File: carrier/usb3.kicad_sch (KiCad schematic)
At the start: 0 parts

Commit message: Feat[carrier]: v3 schematic draft complete
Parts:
- added C25, C26, C30, C31, C32, C37, C40, C41, C42, C43, C44, C45, C48, C51, C52: 10nF, symbol Device:C_Small
- added C3 (x2): 150uF, symbol Device:C_Polarized_Small
- added C38, C39, C46, C47, C49, C50, C54, C55, C56, C57, C58, C59, C9 (x2): 100nF, symbol Device:C_Small
- added C4 (x2), C53: 10uF, symbol Device:C_Small
- added C60, C61: 22pF, symbol Device:C_Small
- added FB1, FB2, FB3: BLM21PG600SN1, symbol Device:FerriteBead_Small
- added J11, J12: USB3_A, symbol Connector:USB3_A
- added R10: 1.6k, symbol Device:R_Small
- added R39: 680, symbol Device:R_Small
- added R40, R43, R45: 10k, symbol Device:R_Small
- added R44: 47k, symbol Device:R_Small
- added R8 (x2): 1M, symbol Device:R_Small
- added U12: uPD720202, Package_DFN_QFN:QFN-48-1EP_7x7mm_P0.5mm_EP5.45x5.45mm, symbol uPD720202:uPD720202
- added U14: W25X40CLUXIG, symbol Memory_Flash:W25X40CLSV
- added U15, U16: AP2191, Package_TO_SOT_SMD:SOT-23-5, symbol AP2191:AP2191
- added U5 (x3): TPD4EUSB30, Package_SON:USON-10_2.5x1.0mm_P0.5mm, symbol CM4IO:TPD4EUSB30
- added Y2: 24MHz, symbol Device:Crystal_GND24_Small
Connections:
- new net: C60.1, R39.1, Y2.3
- new net: C9.1, J12.4 (GND), R8.1
- new net: FB2.2, J11.1 (VBUS)
- new net: C9.1, J11.4 (GND), R8.1
- new net: C56.2, J11.8 (SSTX-)
- new net: C57.2, J11.9 (SSTX+)
- new net: FB3.2, J12.1 (VBUS)
- new net: C58.2, J12.8 (SSTX-)
- new net: C59.2, J12.9 (SSTX+)
- new net: C54.2, U12.4 (PETXP)
- new net: R39.2, U12.23 (XT2)
- new net: C61.1, U12.24 (XT1), Y2.1
- new net: R10.1, U12.26 (RREF)
- new net: C55.2, U12.5 (PETXN)
- new net: R43.2, U14.3 (~{WP})
- new net +1.05v: C39.1, C40.1, C41.1, C42.1, C43.1, C44.1, C45.1, C46.1, C47.1, C48.1, U12.21 (VDD10), U12.30 (VDD10), U12.33 (VDD10), U12.39 (VDD10), U12.42 (VDD10), U12.6 (VDD10), U12.9 (VDD10)
- new net +3.3v: C25.1, C26.1, C30.1, C31.1, C32.1, C37.1, C38.1, FB1.1, R40.2, R43.1, R44.2, R45.2, U12.12 (VDD33), U12.22 (VDD33), U12.34 (VDD33), U12.43 (VDD33), U14.7 (~{HOLD}), U14.8 (VCC)
- new net +5v: U15.5 (IN), U16.5 (IN)
- new net A+3.3v: C49.1, C50.1, C51.1, C52.1, C53.1, FB1.2, U12.25 (AVDD33), U12.3 (AVDD33)
- new net GND: C25.2, C26.2, C3.2, C3.2, C30.2, C31.2, C32.2, C37.2, C38.2, C39.2, C4.2, C4.2, C40.2, C41.2, C42.2, C43.2, C44.2, C45.2, C46.2, C47.2, C48.2, C49.2, C50.2, C51.2, C52.2, C53.2, C60.2, C61.2, C9.2, C9.2, J11.10 (SHIELD), J11.7 (DRAIN), J12.10 (SHIELD), J12.7 (DRAIN), R10.2, R8.2, R8.2, U12.27 (IC(L)), U12.49 (GND_PAD), U14.4 (GND), U15.2 (GND), U16.2 (GND), U5.3 (GND), U5.3 (GND), U5.3 (GND), U5.8 (GND), U5.8 (GND), U5.8 (GND), Y2.2, Y2.4
- new net OCI1B: R40.1, U12.19 (OCI1B), U15.3 (~{FLG})
- new net OCI2B: R45.1, U12.17 (OCI2B), U16.3 (~{FLG})
- new net PECLKN: U12.2 (PECLKN)
- new net PECLKP: U12.1 (PECLKP)
- new net PECREQB: U12.10 (PECREQB)
- new net PERSTB: U12.47 (PERSTB)
- new net PERXN: U12.8 (PERXN)
- new net PERXP: U12.7 (PERXP)
- new net PETXN: C55.1
- new net PETXP: C54.1
- new net PPON1: U12.20 (PPON1), U15.4 (EN)
- new net PPON2: U12.18 (PPON2), U16.4 (EN)
- new net SPICSB: U12.14 (SPICSB), U14.1 (~{CS})
- new net SPISCK: U12.15 (SPISCK), U14.6 (SCK)
- new net SPISI: U12.16 (SPISI), U14.5 (DI(IO0))
- new net SPISO: R44.1, U12.13 (SPISO), U14.2 (DO(IO1))
- new net U2DM1: J12.2 (D-), U12.36 (U2DM1), U5.2 (D1-), U5.9
- new net U2DM2: J11.2 (D-), U12.45 (U2DM2), U5.2 (D1-), U5.9
- new net U2DP1: J12.3 (D+), U12.35 (U2DP1), U5.1 (D1+), U5.10
- new net U2DP2: J11.3 (D+), U12.44 (U2DP2), U5.1 (D1+), U5.10
- new net U3RXDN1: J12.5 (SSRX-), U12.32 (U3RXDN1), U5.5 (D2-), U5.6
- new net U3RXDN2: J11.5 (SSRX-), U12.41 (U3RXDN2), U5.5 (D2-), U5.6
- new net U3RXDP1: J12.6 (SSRX+), U12.31 (U3RXDP1), U5.4 (D2+), U5.7
- new net U3RXDP2: J11.6 (SSRX+), U12.40 (U3RXDP2), U5.4 (D2+), U5.7
- new net U3TXDN1: C58.1, U12.29 (U3TXDN1), U5.5 (D2-), U5.6
- new net U3TXDN2: C56.1, U12.38 (U3TXDN2), U5.2 (D1-), U5.9
- new net U3TXDP1: C59.1, U12.28 (U3TXDP1), U5.4 (D2+), U5.7
- new net U3TXDP2: C57.1, U12.37 (U3TXDP2), U5.1 (D1+), U5.10
- new net VBUS1: C3.1, C4.1, FB3.1, U15.1 (OUT)
- new net VBUS2: C3.1, C4.1, FB2.1, U16.1 (OUT)
- new net nEXTRST: U12.11 (PONRSTB)
- no-connect marks 0 -> 2
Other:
- note added: "@NOTE: PCIe WAKE# is not used"

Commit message: Feat[carrier]: implemented external magnetics, footprints linked
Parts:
- C3: footprint (none) -> Capacitor_SMD:CP_Elec_6.3x7.7
- C39: renamed from C47; footprint (none) -> Capacitor_SMD:C_0402_1005Metric
- C4, C9: footprint (none) -> Capacitor_SMD:C_0402_1005Metric
- C40: renamed from C46; footprint (none) -> Capacitor_SMD:C_0402_1005Metric
- C41: renamed from C38; footprint (none) -> Capacitor_SMD:C_0402_1005Metric
- C42: renamed from C39; footprint (none) -> Capacitor_SMD:C_0402_1005Metric
- C43: renamed from C37; footprint (none) -> Capacitor_SMD:C_0402_1005Metric
- C44: renamed from C40; footprint (none) -> Capacitor_SMD:C_0402_1005Metric
- C45: renamed from C25; footprint (none) -> Capacitor_SMD:C_0402_1005Metric
- C46: renamed from C53; footprint (none) -> Capacitor_SMD:C_0402_1005Metric
- C47: renamed from C61; footprint (none) -> Capacitor_SMD:C_0402_1005Metric
- C48: renamed from C41; footprint (none) -> Capacitor_SMD:C_0402_1005Metric
- C49: renamed from C26; footprint (none) -> Capacitor_SMD:C_0402_1005Metric
- C50: renamed from C42; footprint (none) -> Capacitor_SMD:C_0402_1005Metric
- C51: renamed from C30; footprint (none) -> Capacitor_SMD:C_0402_1005Metric
- C52: renamed from C60; footprint (none) -> Capacitor_SMD:C_0402_1005Metric
- C53: renamed from C43; footprint (none) -> Capacitor_SMD:C_0402_1005Metric
- C54: renamed from C31; footprint (none) -> Capacitor_SMD:C_0402_1005Metric
- C55: renamed from C44; footprint (none) -> Capacitor_SMD:C_0402_1005Metric
- C56: renamed from C32; footprint (none) -> Capacitor_SMD:C_0402_1005Metric
- C57: renamed from C54; footprint (none) -> Capacitor_SMD:C_0402_1005Metric
- C58: renamed from C55; footprint (none) -> Capacitor_SMD:C_0402_1005Metric
- C59: renamed from C45; footprint (none) -> Capacitor_SMD:C_0402_1005Metric
- C60: renamed from C48; footprint (none) -> Capacitor_SMD:C_0402_1005Metric
- C61: renamed from C49; footprint (none) -> Capacitor_SMD:C_0402_1005Metric
- C62: renamed from C50; footprint (none) -> Capacitor_SMD:C_0402_1005Metric
- C63: renamed from C51; footprint (none) -> Capacitor_SMD:C_0402_1005Metric
- C64: renamed from C52; footprint (none) -> Capacitor_SMD:C_0402_1005Metric
- C69: renamed from C56; footprint (none) -> Capacitor_SMD:C_0402_1005Metric
- C70: renamed from C58; footprint (none) -> Capacitor_SMD:C_0402_1005Metric
- C71: renamed from C57; footprint (none) -> Capacitor_SMD:C_0402_1005Metric
- C72: renamed from C59; footprint (none) -> Capacitor_SMD:C_0402_1005Metric
- FB1, FB2, FB3: footprint (none) -> Inductor_SMD:L_0805_2012Metric
- J12: renamed from J11; footprint (none) -> Connector_USB:USB3_A_Molex_48393-001
- J13: renamed from J12; footprint (none) -> Connector_USB:USB3_A_Molex_48393-001
- R43: renamed from R44; footprint (none) -> Resistor_SMD:R_0402_1005Metric
- R44: renamed from R43; footprint (none) -> Resistor_SMD:R_0402_1005Metric
- R45: renamed from R39; footprint (none) -> Resistor_SMD:R_0402_1005Metric
- R46: renamed from R10; footprint (none) -> Resistor_SMD:R_0402_1005Metric
- R47: renamed from R40; footprint (none) -> Resistor_SMD:R_0402_1005Metric
- R48: renamed from R45; footprint (none) -> Resistor_SMD:R_0402_1005Metric
- R8: footprint (none) -> Resistor_SMD:R_0402_1005Metric
- U16: renamed from U14; footprint (none) -> W25X40CLUXIG:W25X40CLUXIG
- Y1: renamed from Y2; footprint (none) -> Crystal:Crystal_SMD_2016-4Pin_2.0x1.6mm
- renumbered U15 to U18, U12 to U19, U16 to U21

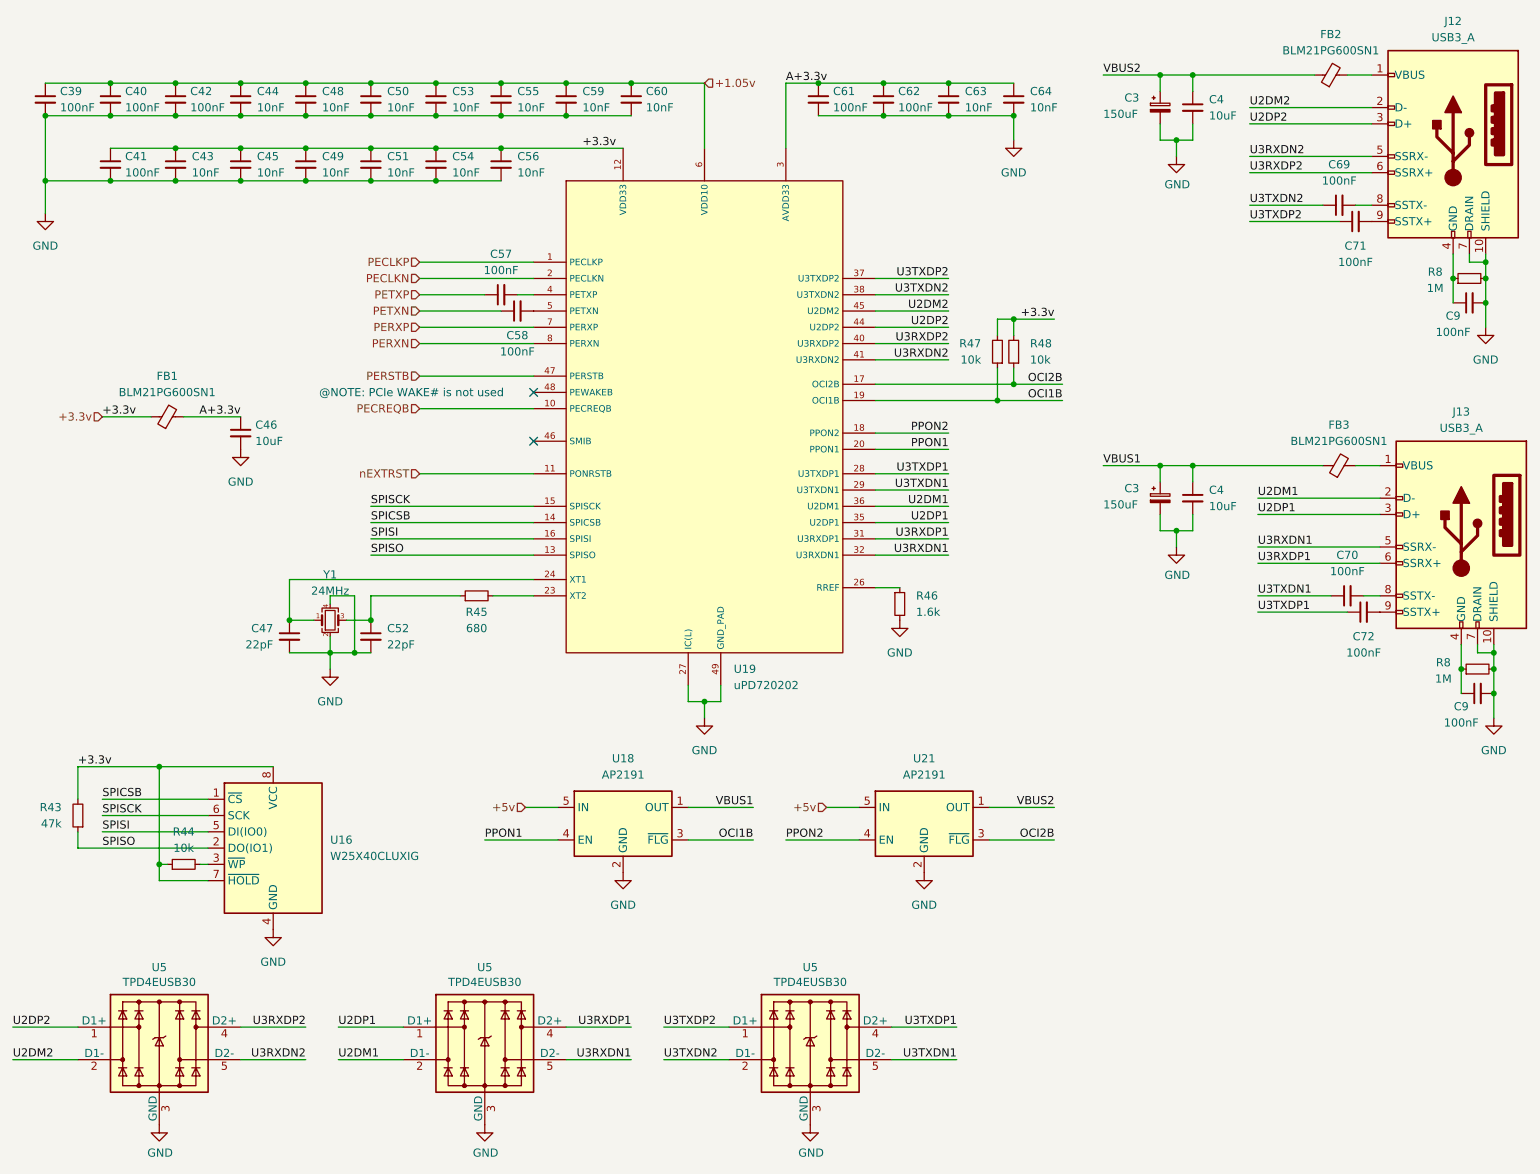
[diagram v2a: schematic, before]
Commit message: Feat[carrier]: v3 board layout complete
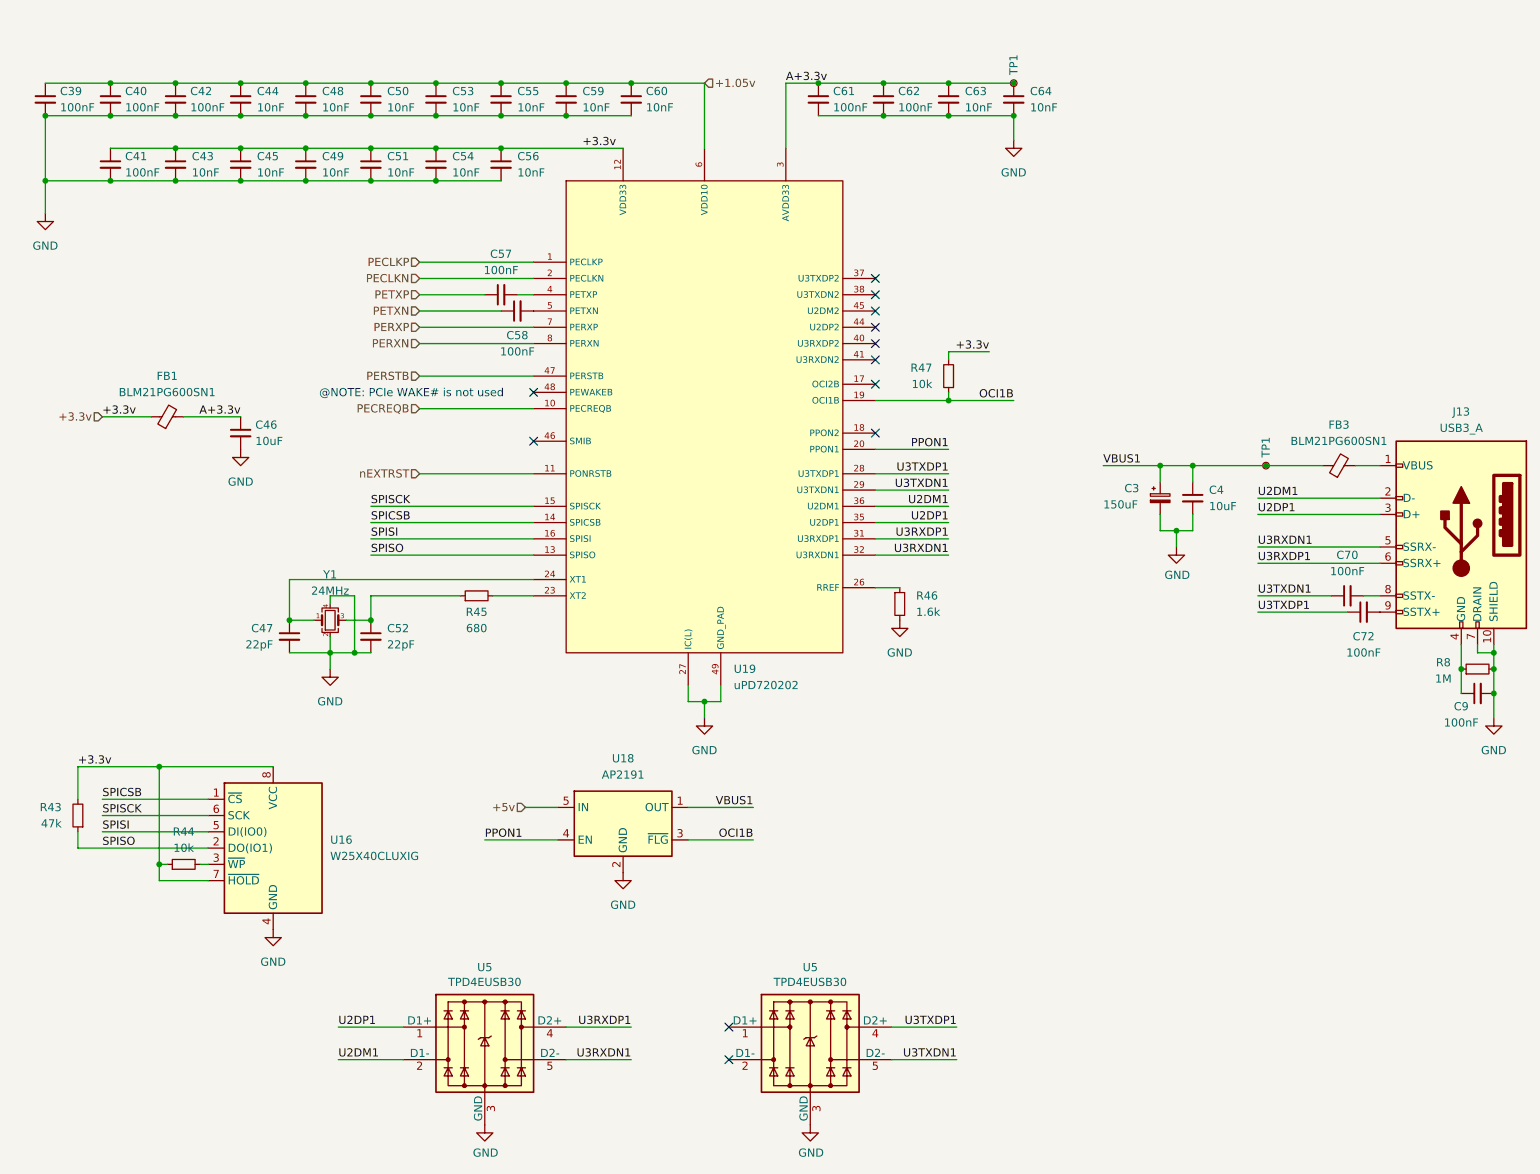
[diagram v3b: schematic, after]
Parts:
- removed C3: 150uF, Capacitor_SMD:CP_Elec_6.3x7.7, symbol Device:C_Polarized_Small
- removed C4: 10uF, Capacitor_SMD:C_0402_1005Metric, symbol Device:C_Small
- removed C69, C71, C9: 100nF, Capacitor_SMD:C_0402_1005Metric, symbol Device:C_Small
- removed FB2: BLM21PG600SN1, Inductor_SMD:L_0805_2012Metric, symbol Device:FerriteBead_Small
- removed J12: USB3_A, Connector_USB:USB3_A_Molex_48393-001, symbol Connector:USB3_A
- removed R48: 10k, Resistor_SMD:R_0402_1005Metric, symbol Device:R_Small
- removed R8: 1M, Resistor_SMD:R_0402_1005Metric, symbol Device:R_Small
- removed U21: AP2191, Package_TO_SOT_SMD:SOT-23-5, symbol AP2191:AP2191
- removed U5: TPD4EUSB30, Package_SON:USON-10_2.5x1.0mm_P0.5mm, symbol CM4IO:TPD4EUSB30
- added TP1 (x2): ~, TestPoint:TestPoint_Pad_D1.5mm, symbol Connector:TestPoint_Small
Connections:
- net A+3.3v: now also TP1.1
- net GND: now also U16.9 (GND)
- net VBUS1: now also TP1.1
- net OCI2B: no longer names the net of U19.17 (OCI2B)
- net PPON2: no longer names the net of U19.18 (PPON2)
- net U2DM2: no longer names the net of U19.45 (U2DM2)
- net U2DP2: no longer names the net of U19.44 (U2DP2)
- net U3RXDN2: no longer names the net of U19.41 (U3RXDN2)
- net U3RXDP2: no longer names the net of U19.40 (U3RXDP2)
- net U3TXDN2: no longer names the net of U5.2 (D1-), U5.9
- net U3TXDN2: no longer U19.38 (U3TXDN2)
- net U3TXDP2: no longer names the net of U5.1 (D1+), U5.10
- net U3TXDP2: no longer U19.37 (U3TXDP2)
- no-connect marks 2 -> 12
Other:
- moved on the sheet: R47

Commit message: Feat[carrier]: routing complete
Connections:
- net SSTX-: now reaches C70.2, J13.8 (SSTX-)
- net SSTX+: now reaches C72.2, J13.9 (SSTX+)
- net PETX+: now reaches C57.2, U19.4 (PETXP)
- net PETX-: now reaches C58.2, U19.5 (PETXN)
- net U2DM1 renamed U2D-
- net U2D-: now also U5.5 (D2-), U5.6; no longer U5.2 (D1-), U5.9
- net U2DP1 renamed U2D+
- net U2D+: now also U5.4 (D2+), U5.7; no longer U5.1 (D1+), U5.10
- net U3RXDN1 renamed U3RXD-
- net U3RXD-: now also U5.2 (D1-), U5.9; no longer U5.5 (D2-), U5.6
- net U3RXDP1 renamed U3RXD+
- net U3RXD+: now also U5.1 (D1+), U5.10; no longer U5.4 (D2+), U5.7
- net U3TXDN1 renamed U3TXD-
- net U3TXDP1 renamed U3TXD+
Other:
- moved on the sheet: C57, C58, C70, C72

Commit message: Feat[carrier]: component mapping complete
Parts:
- R45: footprint Resistor_SMD:R_0402_1005Metric -> Resistor_SMD:R_0603_1608Metric
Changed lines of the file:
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@@
       (effects (font (size 1.27 1.27)))
     )
-    (property "Footprint" "Resistor_SMD:R_0402_1005Metric" (at 92.71 106.68 0)
+    (property "Footprint" "Resistor_SMD:R_0603_1608Metric" (at 92.71 106.68 0)
       (effects (font (size 1.27 1.27)) hide)
     )
